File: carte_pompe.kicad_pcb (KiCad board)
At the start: 2 copper layers, 23 x 23 mm, 14 parts, among them J1 Conn_01x04_Pin, J2 Conn_01x02_Socket, Q1 AO3401A, Q2 AO3401A

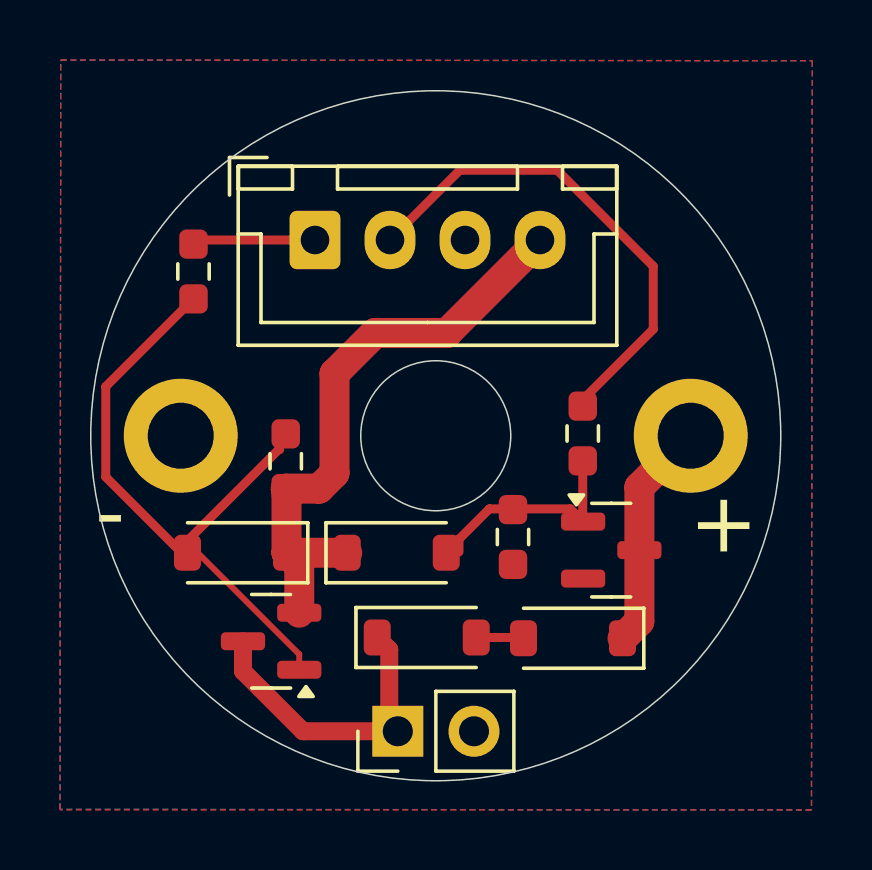
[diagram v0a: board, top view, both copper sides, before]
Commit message: add text
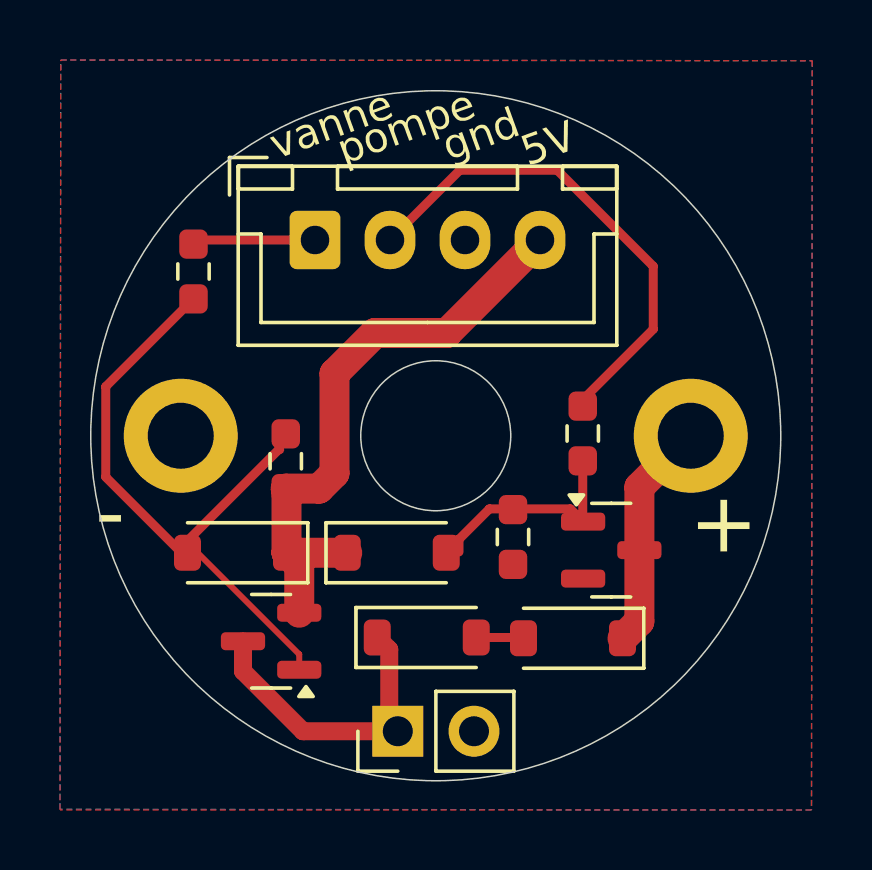
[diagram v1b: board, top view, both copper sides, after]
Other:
- board text added: "5V"
- board text added: "gnd"
- board text added: "pompe"
- board text added: "vanne"
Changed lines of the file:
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@@
 		(tags "SOT TO_SOT_SMD")
 		(property "Reference" "Q1"
-			(at 0 -2.4 360)
+			(at 0 -2.4 0)
 			(layer "F.SilkS")
 			(hide yes)
@@
 		)
 		(property "Value" "AO3401A"
-			(at 0 2.4 360)
+			(at 0 2.4 0)
 			(layer "F.Fab")
 			(hide yes)
@@
 		)
 		(fp_text user "${REFERENCE}"
-			(at 0 0 360)
+			(at 0 0 0)
 			(layer "F.Fab")
 			(effects
@@
 		(tags "SOD-123")
 		(property "Reference" "D3"
-			(at 0 -2 360)
+			(at 0 -2 0)
 			(layer "F.SilkS")
 			(hide yes)
@@
 		)
 		(property "Value" "BZT52C10"
-			(at 0 2.1 360)
+			(at 0 2.1 0)
 			(layer "F.Fab")
 			(hide yes)
@@
 		)
 		(fp_text user "${REFERENCE}"
-			(at 0 -2 360)
+			(at 0 -2 0)
 			(layer "F.Fab")
 			(effects
@@
 		(tags "Through hole pin header THT 1x02 2.54mm single row")
 		(property "Reference" "J2"
-			(at 0 -2.33 270)
+			(at 0 -2.33 -90)
 			(layer "F.SilkS")
 			(hide yes)
@@
 		)
 		(property "Value" "Conn_01x02_Socket"
-			(at 0 4.87 270)
+			(at 0 4.87 -90)
 			(layer "F.Fab")
 			(hide yes)
@@
 		)
 		(fp_text user "${REFERENCE}"
-			(at 0 1.27 360)
+			(at 0 1.27 0)
 			(layer "F.Fab")
 			(effects
@@
 		(tags "resistor handsolder")
 		(property "Reference" "R4"
-			(at 0 -1.43 270)
+			(at 0 -1.43 -90)
 			(layer "F.SilkS")
 			(hide yes)
@@
 		)
 		(property "Value" "20k"
-			(at 0 1.43 270)
+			(at 0 1.43 -90)
 			(layer "F.Fab")
 			(hide yes)
@@
 		)
 		(fp_text user "${REFERENCE}"
-			(at 0 0 270)
+			(at 0 0 -90)
 			(layer "F.Fab")
 			(effects
@@
 		(tags "resistor handsolder")
 		(property "Reference" "R3"
-			(at 0.16 -1.65 270)
+			(at 0.16 -1.65 -90)
 			(layer "F.SilkS")
 			(hide yes)
@@
 		)
 		(property "Value" "20k"
-			(at 0 1.43 270)
+			(at 0 1.43 -90)
 			(layer "F.Fab")
 			(hide yes)
@@
 		)
 		(fp_text user "${REFERENCE}"
-			(at 0 0 270)
+			(at 0 0 -90)
 			(layer "F.Fab")
 			(effects
@@
 		)
 	)
+	(gr_text "gnd"
+		(at 125.475 65.95 20)
+		(layer "F.SilkS")
+		(effects
+			(font
+				(size 1 1)
+				(thickness 0.1)
+			)
+			(justify left bottom)
+		)
+	)
+	(gr_text "5V"
+		(at 128.1 66.125 20)
+		(layer "F.SilkS")
+		(effects
+			(font
+				(size 1 1)
+				(thickness 0.1)
+			)
+			(justify left bottom)
+		)
+	)
 	(gr_text "+"
 		(at 133.45 79.1 0)
@@
 			)
 			(justify left bottom)
+		)
+	)
+	(gr_text "pompe"
+		(at 121.975 66.075 20)
+		(layer "F.SilkS")
+		(effects
+			(font
+				(size 1 1)
+				(thickness 0.1)
+			)
+			(justify left bottom)
+		)
+	)
+	(gr_text "vanne"
+		(at 119.725 65.9 20)
+		(layer "F.SilkS")
+		(effects
+			(font
+				(size 1 1)
+				(thickness 0.1)
+			)
+			(justify left bottom)
